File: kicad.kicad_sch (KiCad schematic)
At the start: 91 parts, among them J1 Conn_01x20_Pin, SW1 CC, SW10 6, SW11 7, SW12 8, SW13 9, SW14 *, SW15 +, SW16 <, SW17 =, SW18 >, SW19 ?, SW2 УС, SW20 @, SW21 A, SW22 B, SW23 C, SW24 D, SW25 E, SW26 F, SW27 G, SW28 H, SW29 I, SW3 УС, SW30 J, SW31 K, SW32 L, SW33 M, SW34 N, SW35 O, SW36 P, SW37 Q, SW38 R, SW39 S, SW4 0, SW40 T, SW41 U, SW42 V, SW43 W, SW44 X, SW45 Y, SW46 Z, SW47 [, SW48 \, SW49 ], SW5 1, SW50 ^, SW51 _, SW52 Space, SW53 Right, SW54 Left, SW55 Up, SW56 Down, SW57 ВК, SW58 СТР, SW59 Home, SW6 2, SW7 3, SW8 4, SW9 5, U1 580вв55, U2 155тм2, U3 155лн1, U4 74LS10

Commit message: add bom and several cosmetic fixes
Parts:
- C3: value 100nF -> 680nF
- SW3: value УС -> РУС
- U2: footprint (none) -> Package_DIP:DIP-14_W7.62mm_LongPads
- U4: value 74LS10 -> 155ла4
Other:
- moved on the sheet: C3, LED2, R14, R3, R5, R6, SW3, U2A, U3A, U3C, U3E, U3F

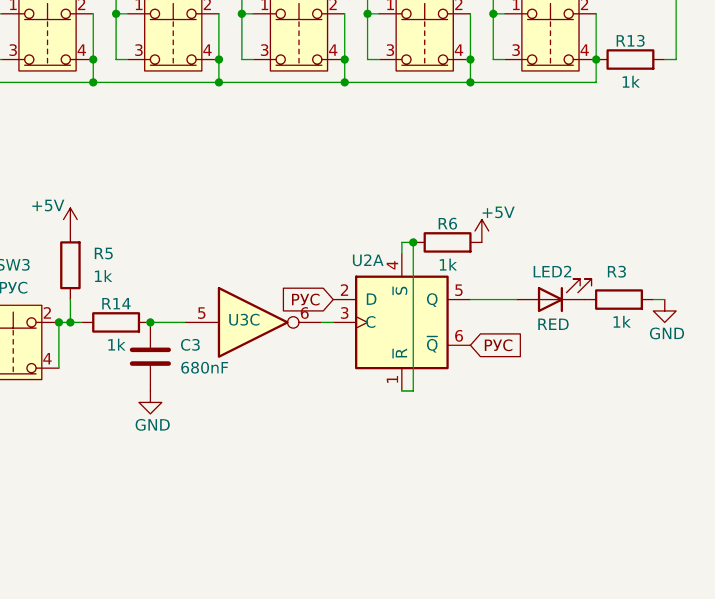
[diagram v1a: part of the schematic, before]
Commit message: add capacitor feature
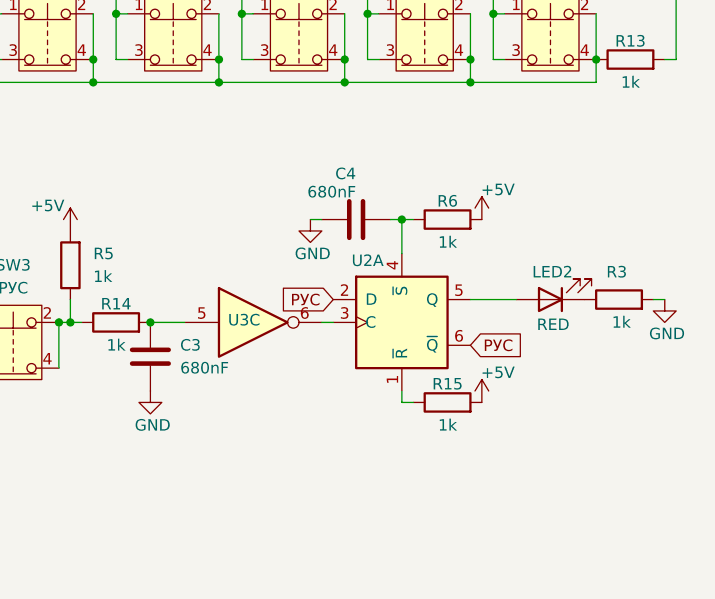
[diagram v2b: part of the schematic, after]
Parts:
- added C4: 680nF, Capacitor_THT:C_Axial_L3.8mm_D2.6mm_P7.50mm_Horizontal, symbol Device:C
- added R15: 1k, Resistor_THT:R_Axial_DIN0411_L9.9mm_D3.6mm_P12.70mm_Horizontal, symbol Device:R
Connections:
- net +5V: now also R15.2
- net GND: now also C4.1
- net at R6.1, U2.4 (~{S}): now also C4.2; no longer U2.1 (~{R})
- new net: R15.1, U2.1 (~{R})
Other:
- moved on the sheet: R6

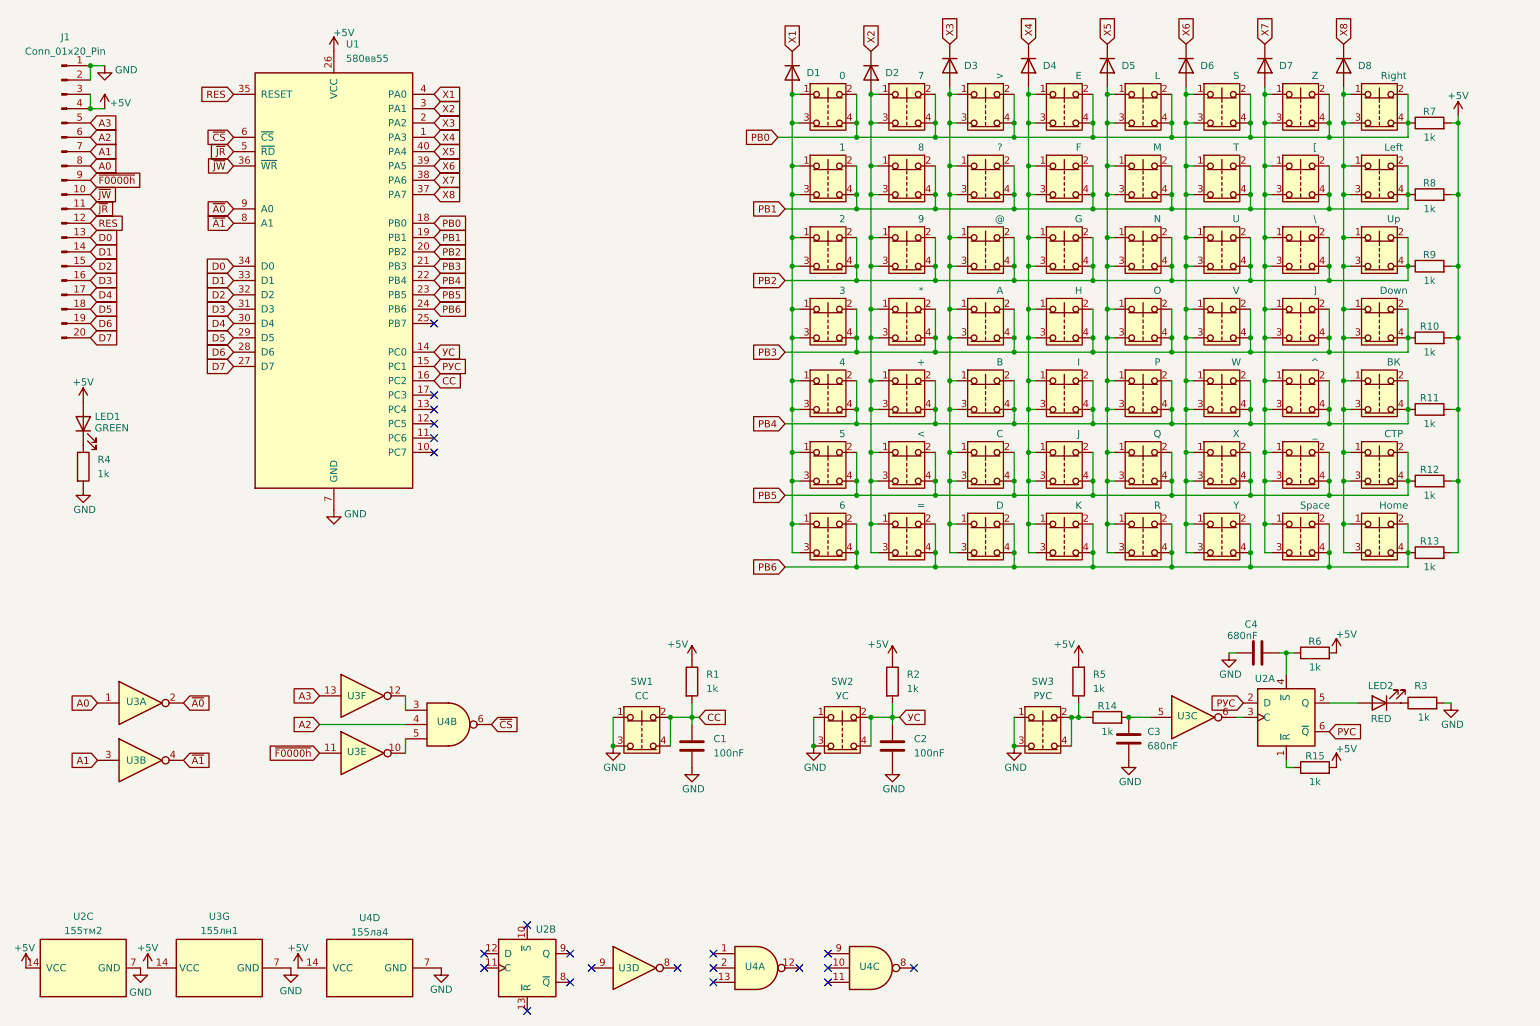
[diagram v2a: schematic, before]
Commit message: change sets of resistors to rn
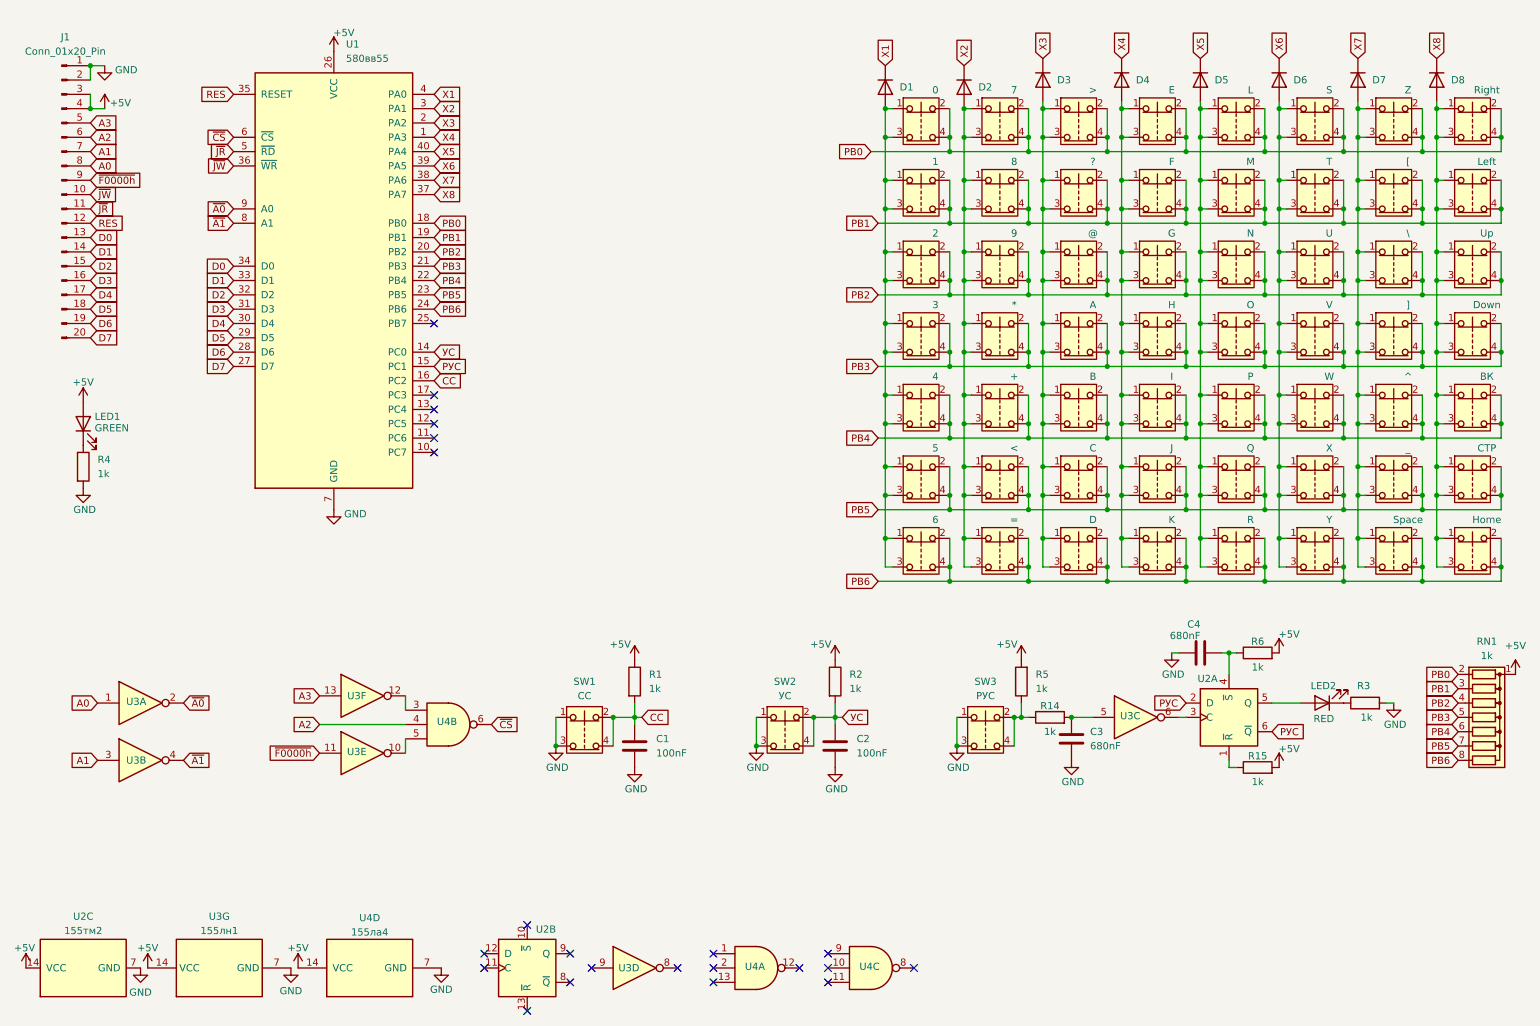
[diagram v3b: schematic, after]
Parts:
- removed R10, R11, R12, R13, R7, R8, R9: 1k, Resistor_THT:R_Axial_DIN0411_L9.9mm_D3.6mm_P12.70mm_Horizontal, symbol Device:R
- added RN1: 1k, Resistor_THT:R_Array_SIP8, symbol Device:R_Network07
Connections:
- net +5V: now also RN1.1 (common)
- net PB0: now also RN1.2 (R1)
- net PB1: now also RN1.3 (R2)
- net PB2: now also RN1.4 (R3)
- net PB3: now also RN1.5 (R4)
- net PB4: now also RN1.6 (R5)
- net PB5: now also RN1.7 (R6)
- net PB6: now also RN1.8 (R7)
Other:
- moved on the sheet: C1, C2, C3, C4, D1, D2, D3, D4, D5, D6, D7, D8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
